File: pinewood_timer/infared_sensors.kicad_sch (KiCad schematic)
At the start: 0 parts

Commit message: worked on schematic more
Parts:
- added D1, D2, D3, D4: LED, LED_THT:LED_D5.0mm, symbol Device:LED
- added PT1, PT2, PT3, PT4: ~, LED_THT:LED_D5.0mm, symbol 2N4403:PT204-6B
- added R33, R36, R38, R40: 56KΩ, symbol Device:R_Small_US
- added R34, R35, R37, R39: 220Ω, symbol Device:R_Small_US
- added R41, R42, R43, R44: 1KΩ, symbol Device:R_Small_US
- added RV1: 10k pot, symbol Device:R_Potentiometer_US
- added U10: LM339N, N14, symbol LM339:LM339N
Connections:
- new net: D4.2 (A), R39.2
- new net: D2.2 (A), R35.2
- new net: D3.2 (A), R37.2
- new net: D1.2 (A), R34.2
- new net +3.3V: PT1.1 (+), PT2.1 (+), PT3.1 (+), PT4.1 (+), R34.1, R35.1, R37.1, R39.1, R41.1, R42.1, R43.1, R44.1
- new net +5V: RV1.1, U10.3 (VCC)
- new net GND: D1.1 (K), D2.1 (K), D3.1 (K), D4.1 (K), R33.2, R36.2, R38.2, R40.2, RV1.3, U10.12 (GND)
- new net V_OUT1: R41.2, U10.1 (1OUT)
- new net V_OUT2: R42.2, U10.2 (2OUT)
- new net V_OUT3: R43.2, U10.14 (OUT3)
- new net V_OUT4: R44.2, U10.13 (OUT4)
- new net V_PT1: PT1.2 (-), R33.1, U10.7 (1IN+)
- new net V_PT2: PT2.2 (-), R36.1, U10.5 (2IN+)
- new net V_PT3: PT3.2 (-), R38.1, U10.9 (3IN+)
- new net V_PT4: PT4.2 (-), R40.1, U10.11 (4IN+)
- new net pot: RV1.2, U10.10 (4IN-), U10.4 (2IN-), U10.6 (1IN-), U10.8 (3IN-)
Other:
- note added: "this wont be a pot forever, it is jsut to adjust for the distance. afterwards, the resistor value will be taken and the pot will be replaced"
- title: (none) -> IR SENSORS

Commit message: added pins
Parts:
- added J1: Conn_01x07_Pin, symbol Connector:Conn_01x06_Pin
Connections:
- net +5V: now also J1.5 (Pin_5)
- net GND: now also J1.6 (Pin_6)
- net V_OUT1: now also J1.1 (Pin_1)
- net V_OUT2: now also J1.2 (Pin_2)
- net V_OUT3: now also J1.3 (Pin_3)
- net V_OUT4: now also J1.4 (Pin_4)
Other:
- note added: "PA11"
- note added: "PA12"
- note added: "PA13"
- note added: "PA14"

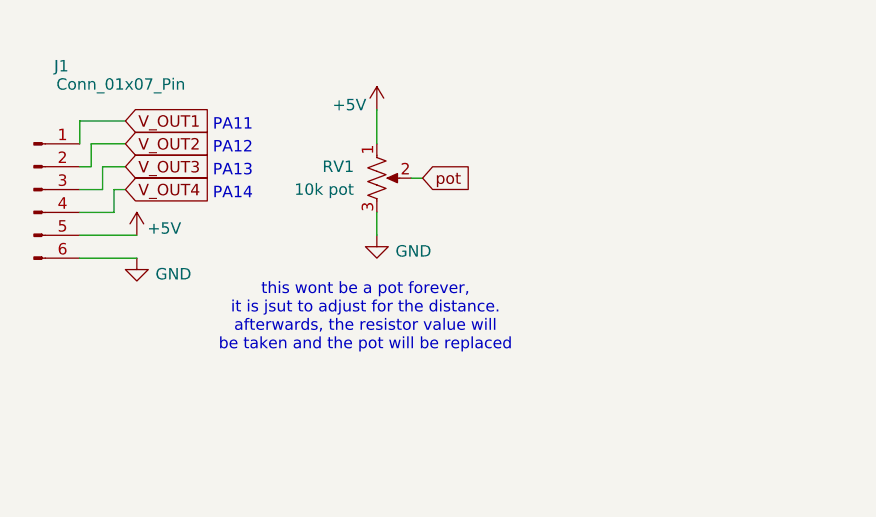
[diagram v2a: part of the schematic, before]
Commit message: edited placement timer schematic since i can never make up my mind
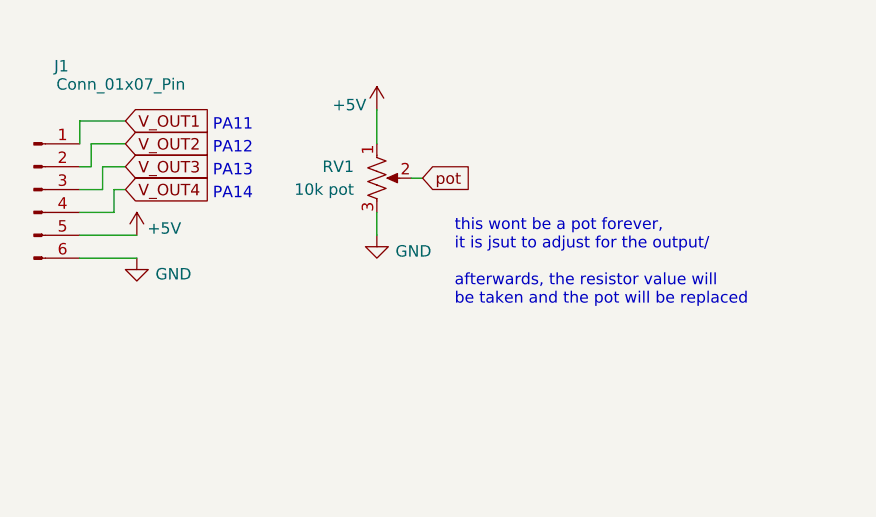
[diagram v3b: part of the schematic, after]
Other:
- note added: "this wont be a pot forever, it is jsut to adjust for the output/ afterwards, the resistor value will be taken and the pot will be replaced"
- note removed: "this wont be a pot forever, it is jsut to adjust for the distance. afterwards, the resistor value will be taken and the pot will be replaced"
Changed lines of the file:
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@@
 		)
 	)
-	(text "this wont be a pot forever, \nit is jsut to adjust for the distance.\nafterwards, the resistor value will\nbe taken and the pot will be replaced"
+	(text "this wont be a pot forever, \nit is jsut to adjust for the output/\n\nafterwards, the resistor value will\nbe taken and the pot will be replaced"
 		(exclude_from_sim no)
-		(at 143.51 95.504 0)
+		(at 153.416 84.582 0)
 		(effects
 			(font
 				(size 1.27 1.27)
 			)
+			(justify left top)
 		)
 	)

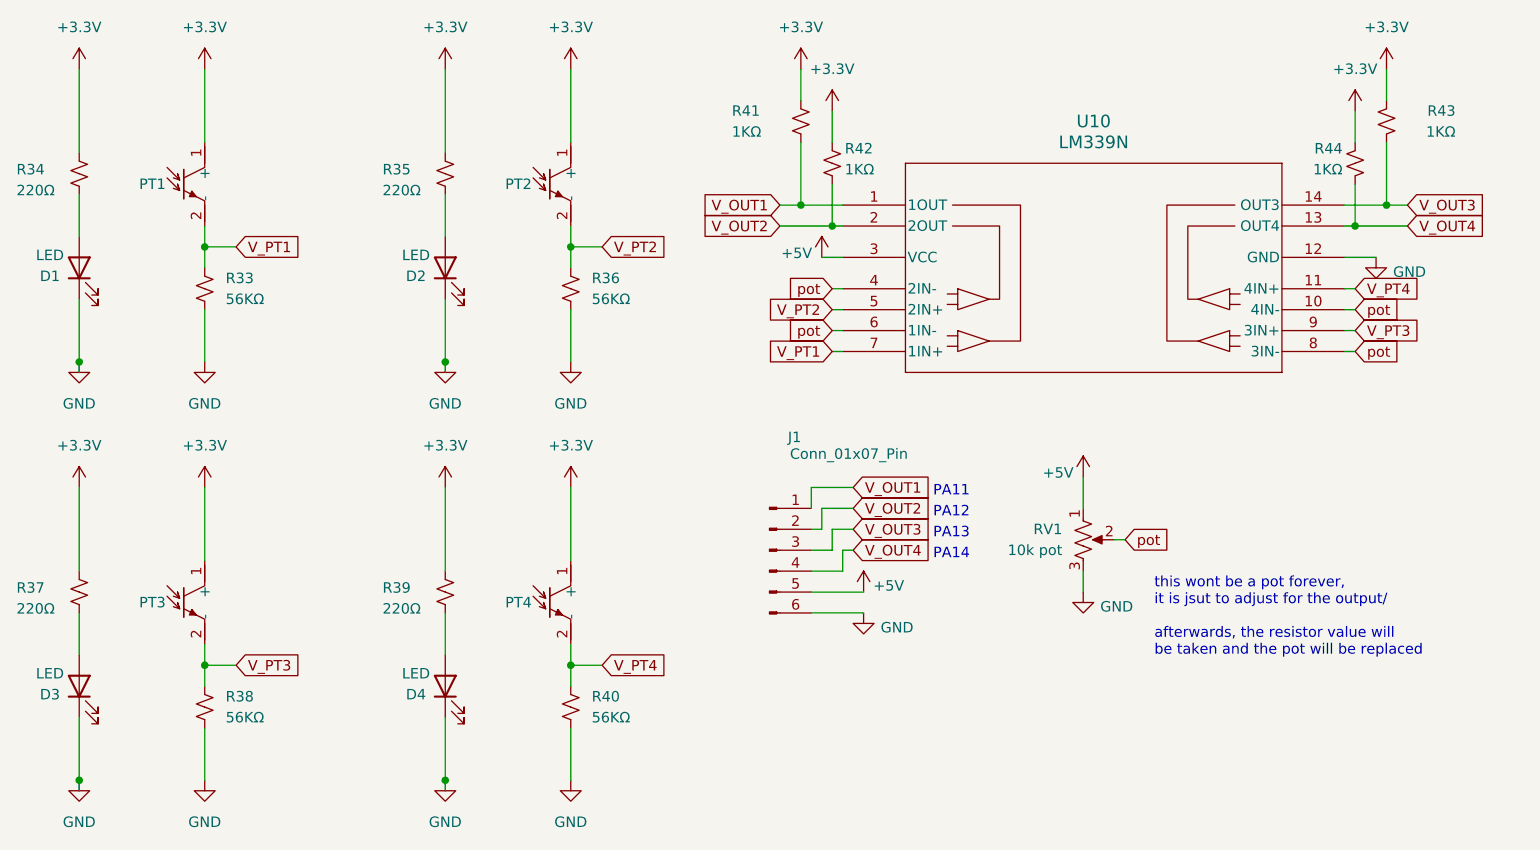
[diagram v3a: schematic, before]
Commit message: keep forgetting ot push - a lot of updates
fixed stm pinout. needs a lot more support than i was providing
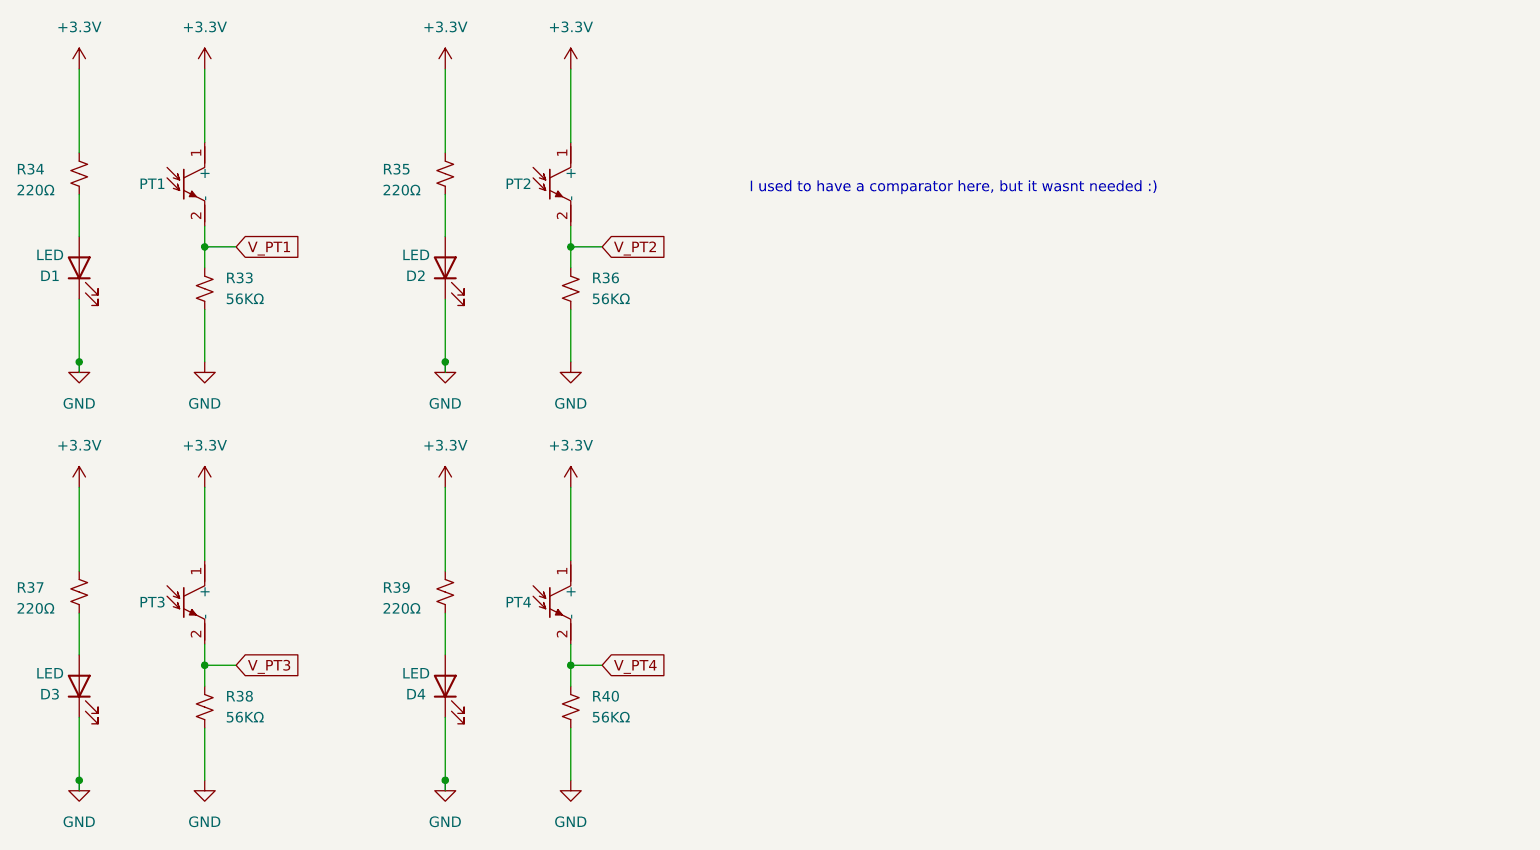
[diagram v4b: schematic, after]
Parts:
- removed J1: Conn_01x07_Pin, symbol Connector:Conn_01x06_Pin
- removed R41, R42, R43, R44: 1KΩ, symbol Device:R_Small_US
- removed RV1: 10k pot, symbol Device:R_Potentiometer_US
- removed U10: LM339N, N14, symbol LM339:LM339N
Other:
- note added: "I used to have a comparator here, but it wasnt needed :)"
- note removed: "PA11"
- note removed: "PA12"
- note removed: "PA13"
- note removed: "PA14"
- note removed: "this wont be a pot forever, it is jsut to adjust for the output/ afterwards, the resistor value will be taken and the pot will be replaced"
